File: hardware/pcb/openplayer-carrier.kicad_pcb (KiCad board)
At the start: 2 copper layers, 60 x 45 mm, 15 parts, among them J1 Pi_40pin_IDC, J2 PWR_IN, J3 KEY, J4 BUTTONS, J5 DISPLAY, J6 SWITCH

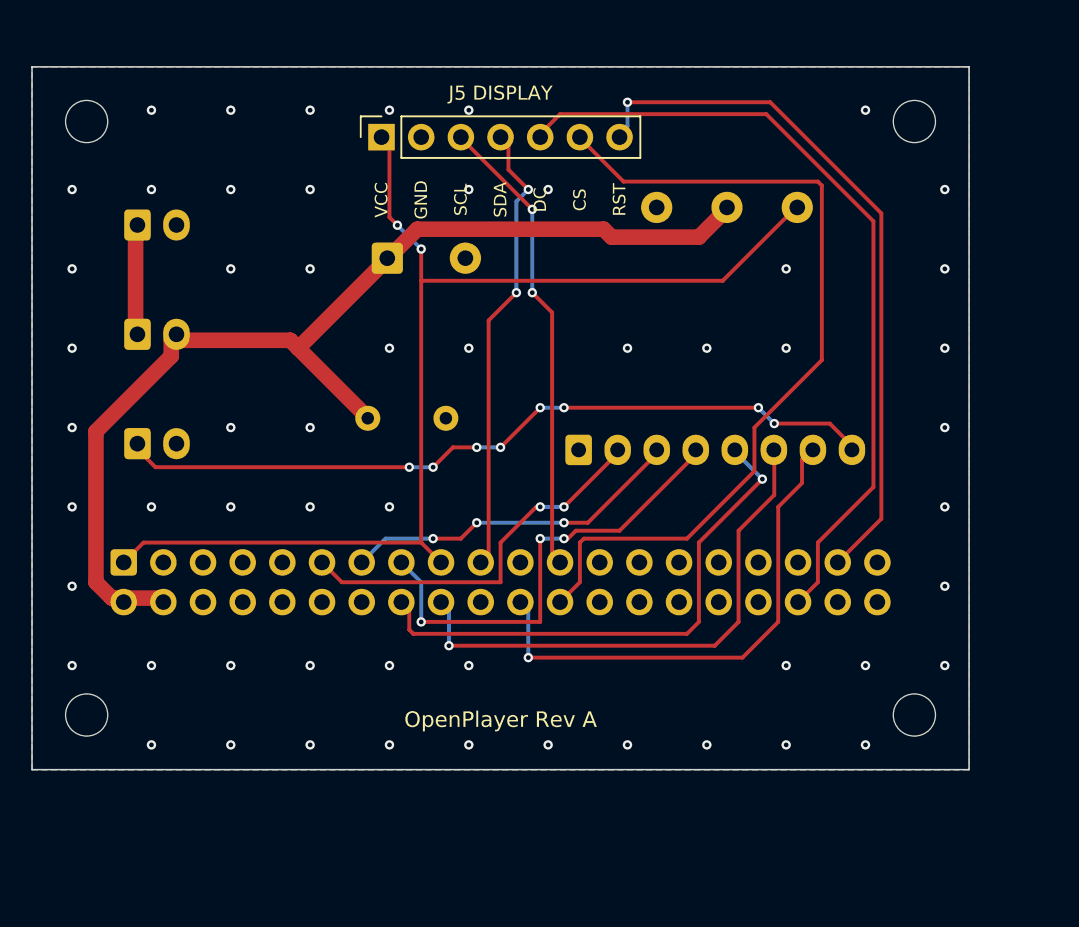
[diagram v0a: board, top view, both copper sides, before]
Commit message: Refactor PCB layout for Rev B: adjust dimensions, reposition components, and implement C1 body outline with keep-out area
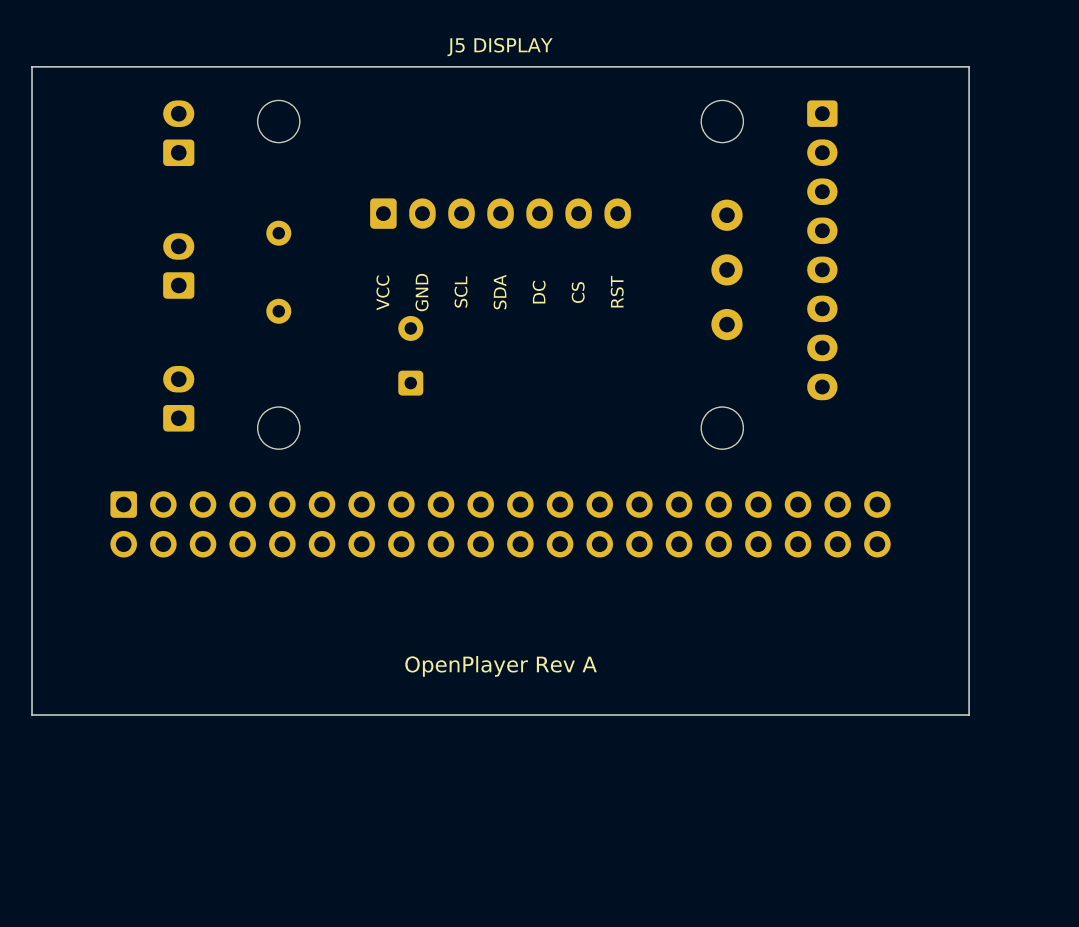
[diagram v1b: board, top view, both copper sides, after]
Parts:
- C1: value 1000uF 10V -> 470uF 10V; footprint Capacitor_THT:CP_Radial_D10.0mm_P5.00mm -> Capacitor_THT:CP_Radial_D8.0mm_P3.50mm
- J1: footprint Connector_IDC:IDC-Header_2x20_P2.54mm_Vertical -> Connector_IDC:IDC-Header_2x20_P2.54mm_Horizontal
- J2, J3, J6: footprint Connector_JST:JST_XH_B2B-XH-A_1x02_P2.50mm_Vertical -> Connector_JST:JST_XH_S2B-XH-A_1x02_P2.50mm_Horizontal
- J4: footprint Connector_JST:JST_XH_B8B-XH-A_1x08_P2.50mm_Vertical -> Connector_JST:JST_XH_S8B-XH-A_1x08_P2.50mm_Horizontal
- J5: footprint Connector_PinSocket_2.54mm:PinSocket_1x07_P2.54mm_Vertical -> Connector_JST:JST_XH_S7B-XH-A_1x07_P2.50mm_Horizontal; moved to B.Cu
- moved J4 26.6 mm to (150.6, 103.0), turned to -90 degrees
- moved H3 22.1 mm to (115.8, 123.1)
- moved H4 22.1 mm to (144.2, 123.1)
- moved H1 12.3 mm to (115.8, 103.5)
- moved H2 12.3 mm to (144.2, 103.5)
- moved C2 8.91 mm to (115.8, 115.7), turned to 90 degrees
- moved TP3 8.75 mm to (144.5, 116.5)
- moved C1 8.14 mm to (124.3, 120.2), turned to 90 degrees
- moved J2 5.33 mm to (109.4, 105.5), turned to 90 degrees
- moved J5 4.90 mm to (122.5, 109.4), turned to 0 degrees
- moved TP1 4.53 mm to (144.5, 109.5)
- moved J6 4.09 mm to (109.4, 114.0), turned to 90 degrees
- moved TP2 4.00 mm to (144.5, 113.0)
- moved J1 3.70 mm to (105.9, 128.0)
- moved J3 3.10 mm to (109.4, 122.5), turned to 90 degrees
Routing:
- net /3V3: track 74.4 -> 0.00 mm, vias 2 -> 0
- net /5V_SYS: track 69.3 -> 0.00 mm
- net /LCD_CS: track 54.3 -> 0.00 mm
- net /LCD_DC: track 51.2 -> 0.00 mm
- net /PWR_KEY: track 49.3 -> 0.00 mm, vias 8 -> 0
- net /LCD_RST: track 45.1 -> 0.00 mm, vias 1 -> 0
- net /BTN_VOLUP: track 34.4 -> 0.00 mm, vias 1 -> 0
- net /BTN_VOLDN: track 34.1 -> 0.00 mm, vias 1 -> 0
- net /BTN_MENU: track 32.7 -> 0.00 mm, vias 1 -> 0
- net /SPI_SCLK: track 29.8 -> 0.00 mm, vias 2 -> 0
- net /BTN_NEXT: track 29.7 -> 0.00 mm, vias 3 -> 0
- net /SPI_MOSI: track 29.2 -> 0.00 mm, vias 2 -> 0
- net /BTN_PLAY: track 24.5 -> 0.00 mm, vias 2 -> 0
- net /BTN_PREV: track 22.0 -> 0.00 mm, vias 3 -> 0
- net /5V_IN: track 7.04 -> 0.00 mm
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- removed copper zone on B.Cu, net /GND
- removed copper zone on F.Cu, net /GND
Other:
- board size 60 x 45 mm -> 60 x 41.5 mm

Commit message: Implement code changes to enhance functionality and improve performance
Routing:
- net /PWR_KEY: track 0.00 -> 75.4 mm, vias 0 -> 4
- net /5V_SYS: track 0.00 -> 65.6 mm
- net /BTN_PLAY: track 0.00 -> 65.0 mm
- net /3V3: track 0.00 -> 62.7 mm, vias 0 -> 2
- net /BTN_VOLDN: track 0.00 -> 56.9 mm, vias 0 -> 2
- net /BTN_VOLUP: track 0.00 -> 56.4 mm, vias 0 -> 2
- net /BTN_PREV: track 0.00 -> 52.5 mm, vias 0 -> 3
- net /BTN_MENU: track 0.00 -> 49.9 mm, vias 0 -> 2
- net /LCD_CS: track 0.00 -> 45.0 mm
- net /SPI_SCLK: track 0.00 -> 42.3 mm
- net /LCD_DC: track 0.00 -> 38.9 mm
- net /BTN_NEXT: track 0.00 -> 37.7 mm, vias 0 -> 3
- net /LCD_RST: track 0.00 -> 34.8 mm, vias 0 -> 1
- net /SPI_MOSI: track 0.00 -> 19.6 mm, vias 0 -> 4
- net /5V_IN: track 0.00 -> 10.7 mm
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- added copper zone on B.Cu, net /GND
- added copper zone on F.Cu, net /GND

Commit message: Refactor silkscreen function in build_pcb.py for improved readability and maintainability
- Introduced a new helper function `pads` to streamline the retrieval of connector pad positions.
- Updated the silkscreen labeling logic for connectors J4 and J5 to enhance clarity and organization.
- Adjusted text positioning for better alignment and visibility on the PCB.
- Changed references from "Rev A" to "Rev B" in the text labels to reflect the latest version.
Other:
- board text added: "OpenPlayer Rev B"
- board text added: "OpenPlayer carrier Rev B"
- board text removed: "OpenPlayer Rev A"
- board text removed: "OpenPlayer carrier Rev A"

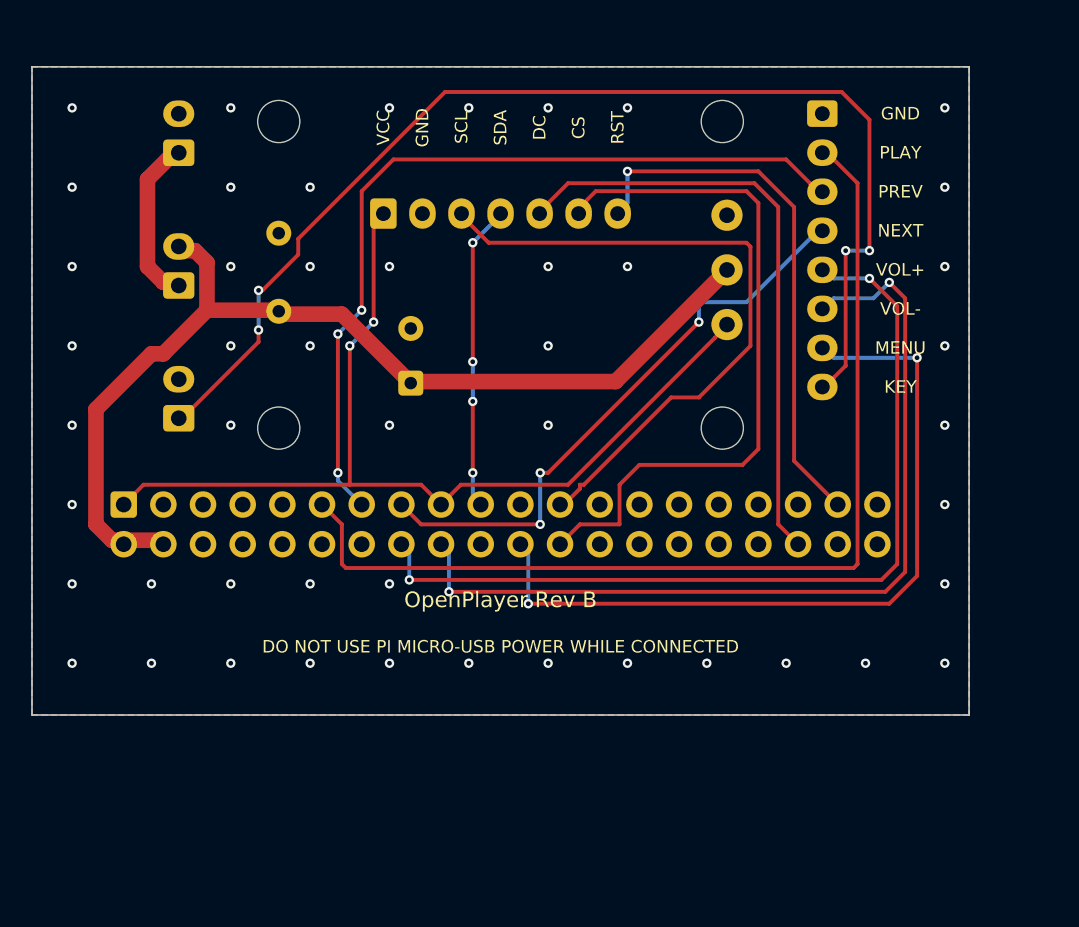
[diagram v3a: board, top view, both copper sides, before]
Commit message: Update PCB design for Rev C: integrate Pi Zero, adjust dimensions, and enhance layout
- Changed board dimensions to accommodate Pi Zero and GC9A01 module.
- Updated component placements and added new connectors for improved accessibility.
- Implemented new functions for Pi overlay and display outline.
- Added DRC rules for display standoffs and antenna keepout area.
- Enhanced documentation and comments for clarity on design changes.
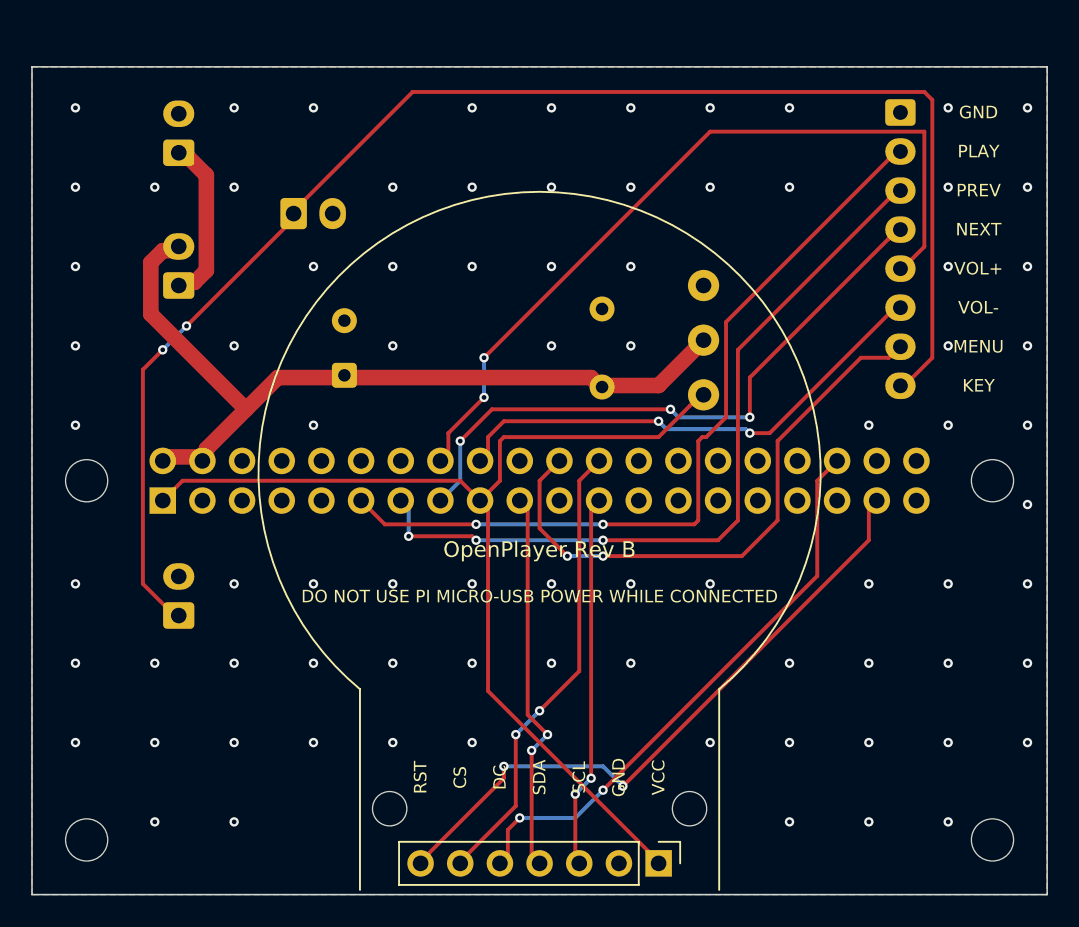
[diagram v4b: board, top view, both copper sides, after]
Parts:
- added H5: M2, MountingHole:MountingHole_2.2mm_M2, F.Cu at (122.9, 147.5)
- added H6: M2, MountingHole:MountingHole_2.2mm_M2, F.Cu at (142.1, 147.5)
- added J7: PWR_BTN, Connector_JST:JST_XH_S2B-XH-A_1x02_P2.50mm_Horizontal, B.Cu at (116.8, 109.4)
- J1: value Pi_40pin_IDC -> Pi_40pin_socket; footprint Connector_IDC:IDC-Header_2x20_P2.54mm_Horizontal -> Connector_PinSocket_2.54mm:PinSocket_2x20_P2.54mm_Vertical
- J5: footprint Connector_JST:JST_XH_S7B-XH-A_1x07_P2.50mm_Horizontal -> Connector_PinHeader_2.54mm:PinHeader_1x07_P2.54mm_Vertical; moved to F.Cu
- moved J5 45.2 mm to (140.1, 151.0), turned to -90 degrees
- moved H4 31.5 mm to (161.5, 149.5)
- moved H3 29.1 mm to (103.5, 149.5)
- moved H2 28.8 mm to (161.5, 126.5)
- moved H1 26.1 mm to (103.5, 126.5)
- moved C2 21.3 mm to (136.5, 120.5)
- moved J3 12.6 mm to (109.4, 135.1)
- moved J4 5.00 mm to (155.6, 102.9)
- moved TP1 4.74 mm to (143.0, 114.0)
- moved TP2 4.74 mm to (143.0, 117.5)
- moved TP3 4.74 mm to (143.0, 121.0)
- moved C1 4.28 mm to (120.0, 119.8)
- moved J1 2.51 mm to (108.4, 127.8)
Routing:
- net /BTN_VOLDN: track 56.9 -> 32.1 mm
- net /PWR_KEY: track 75.4 -> 94.3 mm, vias 4 -> 2
- net /SPI_SCLK: track 42.3 -> 23.9 mm, vias 0 -> 2
- net /LCD_CS: track 45.0 -> 29.4 mm, vias 0 -> 2
- net /BTN_PLAY: track 65.0 -> 51.5 mm, vias 0 -> 2
- net /BTN_MENU: track 49.9 -> 37.2 mm
- net /5V_SYS: track 65.6 -> 53.1 mm
- net /LCD_RST: track 34.8 -> 41.6 mm, vias 1 -> 2
- net /3V3: track 62.7 -> 67.9 mm, vias 2 -> 0
- net /SPI_MOSI: track 19.6 -> 24.6 mm, vias 4 -> 2
- net /BTN_VOLUP: track 56.4 -> 51.4 mm
- net /BTN_PREV: track 52.5 -> 49.7 mm
- net /BTN_NEXT: track 37.7 -> 40.0 mm
- net /LCD_DC: track 38.9 -> 36.8 mm, vias 0 -> 2
- net /GND: vias 48 -> 81
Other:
- board size 60 x 41.5 mm -> 65 x 53 mm

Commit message: Fix PCB layout and silkscreen labels for OpenPlayer carrier Rev C
- Adjusted placement of component C2 for better alignment.
- Updated NAMES dictionary to include J7 (PWR_BTN).
- Modified silkscreen text positioning for J4 and J5 to enhance visibility.
- Changed version label from Rev B to Rev C and updated related text.
- Added warning text regarding the use of the Pi micro-USB power.
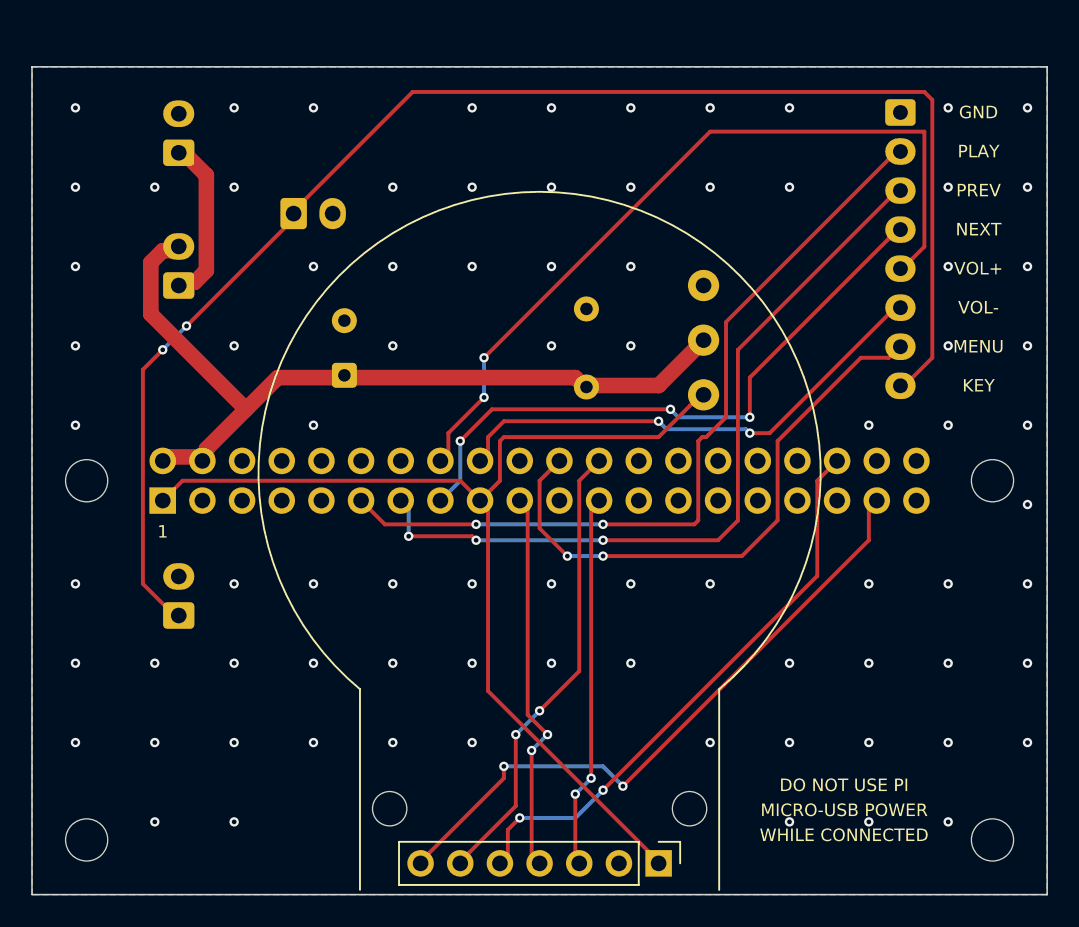
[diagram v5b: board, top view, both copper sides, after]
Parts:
- moved C2 1.00 mm to (135.5, 120.5)
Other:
- board text added: "1"
- board text added: "DO NOT USE PI"
- board text added: "J5 DISPLAY (VCC ◂)"
- board text added: "J7 PWR_BTN"
- board text added: "MICRO-USB POWER"
- board text added: "OpenPlayer carrier Rev C"
- board text added: "PI ZERO ▾"
- board text added: "WHILE CONNECTED"
- board text removed: "DO NOT USE PI MICRO-USB POWER WHILE CONNECTED"
- board text removed: "J5 DISPLAY"
- board text removed: "OpenPlayer Rev B"
- board text removed: "OpenPlayer carrier Rev B"
